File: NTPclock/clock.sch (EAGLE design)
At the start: 27 parts, among them IC1 MAX7219CNG

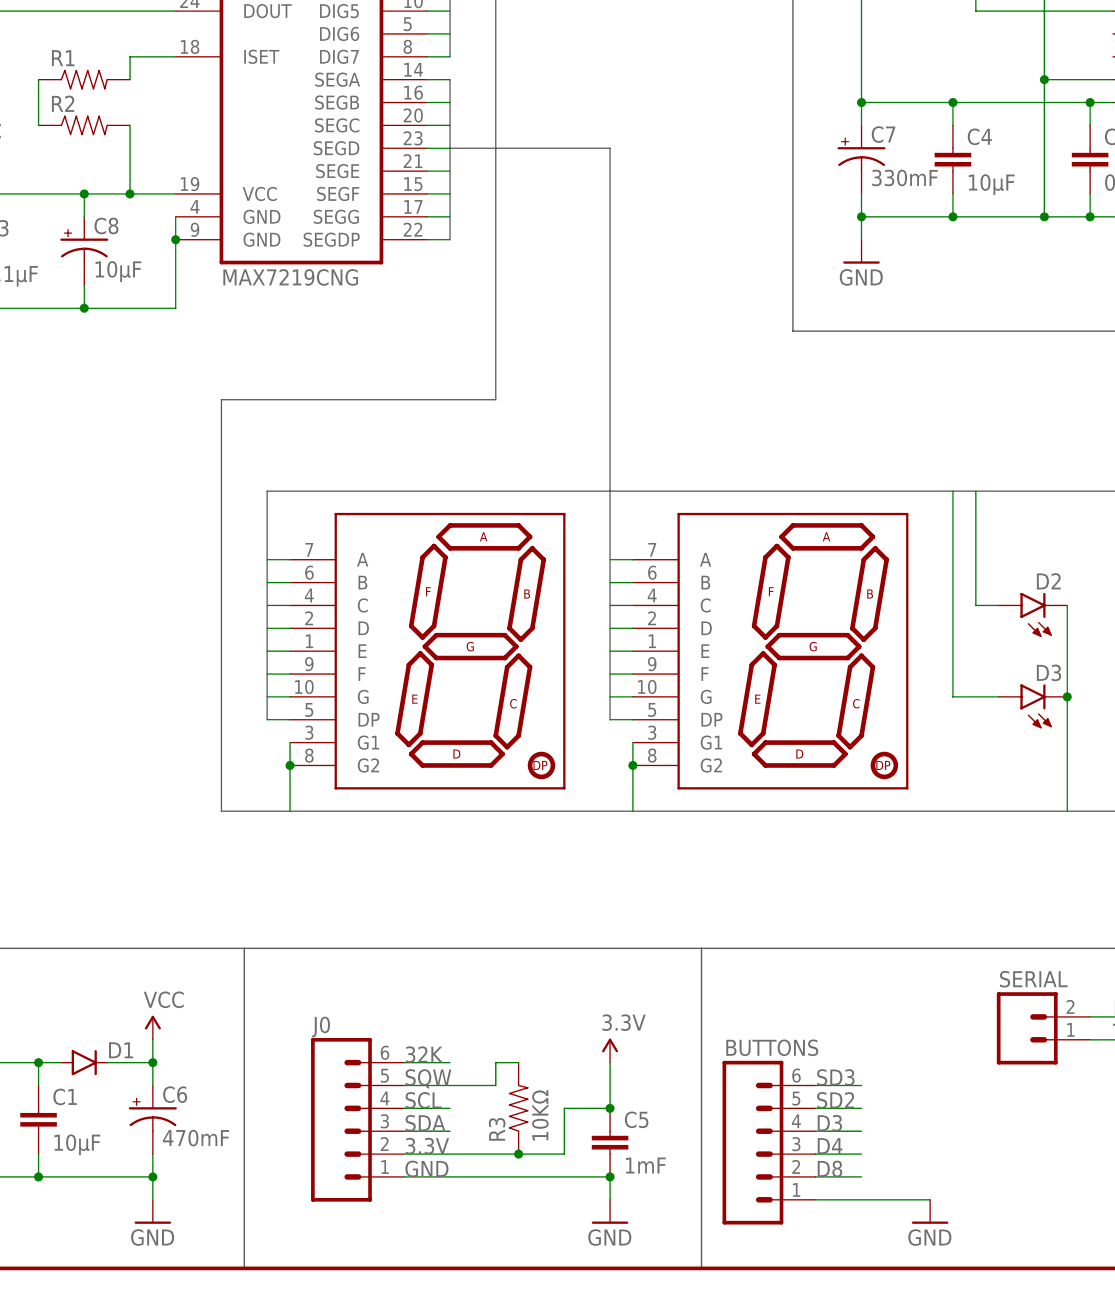
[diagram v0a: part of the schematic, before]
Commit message: Unit fixes
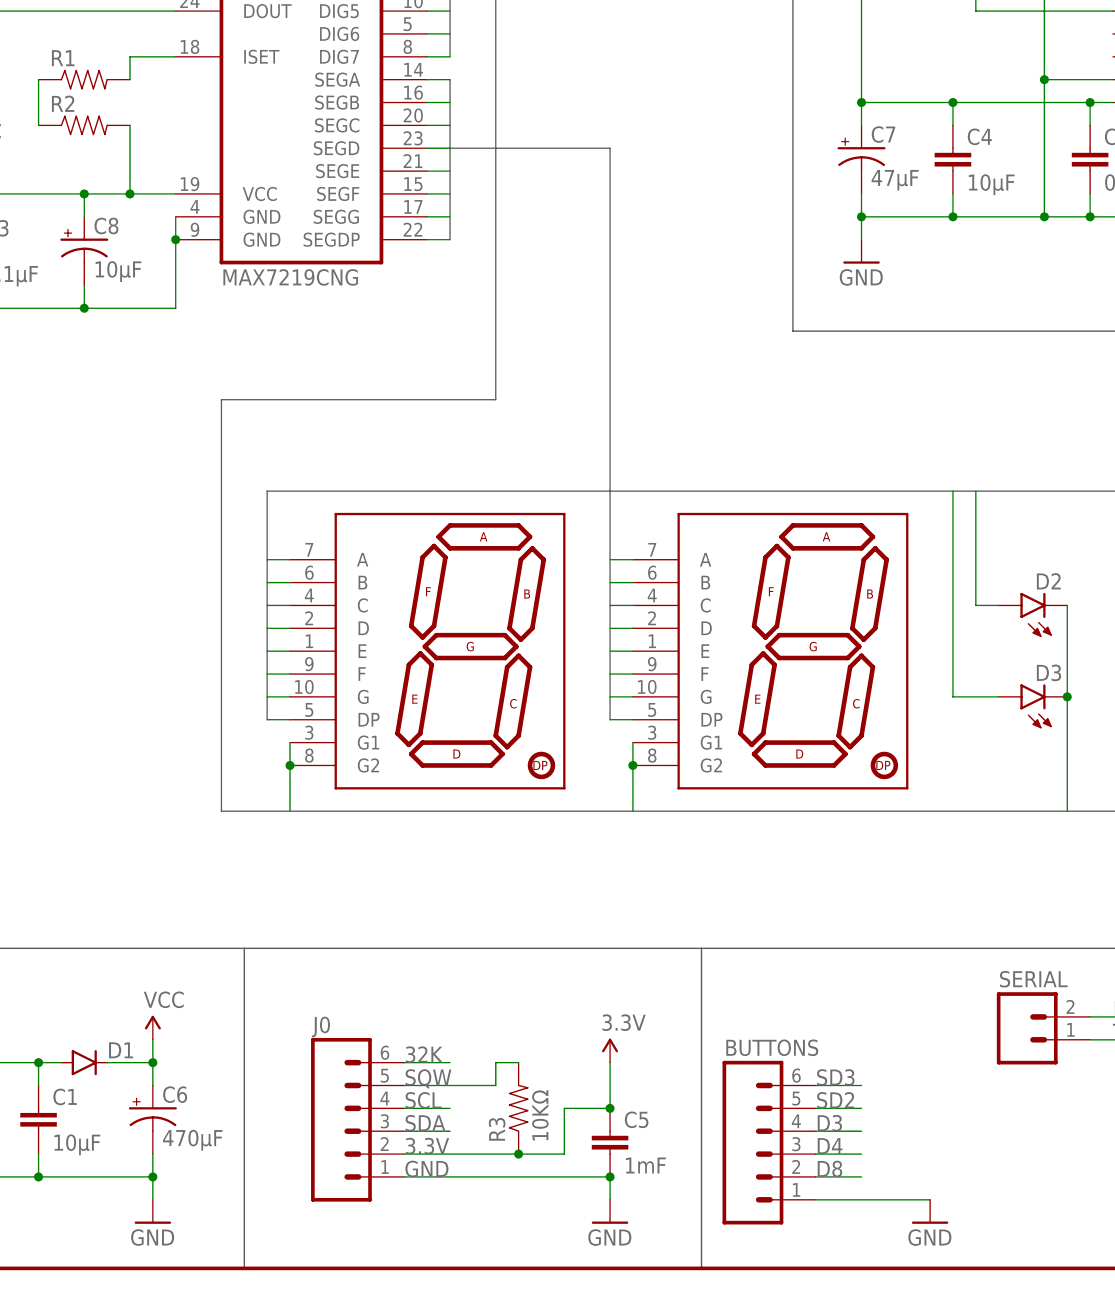
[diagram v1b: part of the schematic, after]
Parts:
- C6: value 470mF -> 470μF
- C7: value 330mF -> 47μF
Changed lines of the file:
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@@
 <part name="C4" library="SparkFun-Capacitors" deviceset="CAP" device="1206" value="10μF"/>
 <part name="C5" library="SparkFun-Capacitors" deviceset="CAP" device="1206" value="1mF"/>
-<part name="C6" library="SparkFun-Capacitors" deviceset="CAP_POL" device="PTH1" value="470mF"/>
-<part name="C7" library="SparkFun-Capacitors" deviceset="CAP_POL" device="PTH1" value="330mF"/>
+<part name="C6" library="SparkFun-Capacitors" deviceset="CAP_POL" device="PTH1" value="470μF"/>
+<part name="C7" library="SparkFun-Capacitors" deviceset="CAP_POL" device="PTH1" value="47μF"/>
 <part name="C8" library="SparkFun-Capacitors" deviceset="CAP_POL" device="PTH1" value="10μF"/>
 <part name="POWER" library="SparkFun-Connectors" deviceset="M02" device="JST-PTH-VERT"/>

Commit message: Add v1.0 logo to board
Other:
- note added: "1.0"
- note removed: "1.1"
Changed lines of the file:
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@@
 <wire x1="215.9" y1="53.34" x2="129.54" y2="53.34" width="0.1524" layer="97"/>
 <wire x1="129.54" y1="53.34" x2="129.54" y2="134.62" width="0.1524" layer="97"/>
-<text x="264.16" y="-43.18" size="1.778" layer="97">1.1</text>
+<text x="264.16" y="-43.18" size="1.778" layer="97">1.0</text>
 <text x="193.04" y="-43.18" size="1.778" layer="97">Joshua Villwock</text>
 <wire x1="215.9" y1="134.62" x2="215.9" y2="53.34" width="0.1524" layer="97"/>

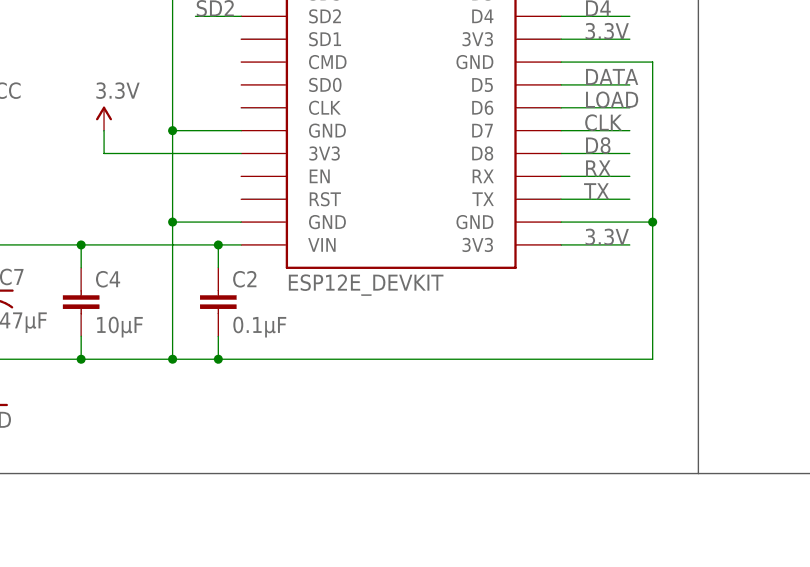
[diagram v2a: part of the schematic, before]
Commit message: Begin updating the Board file for the cheaper V3
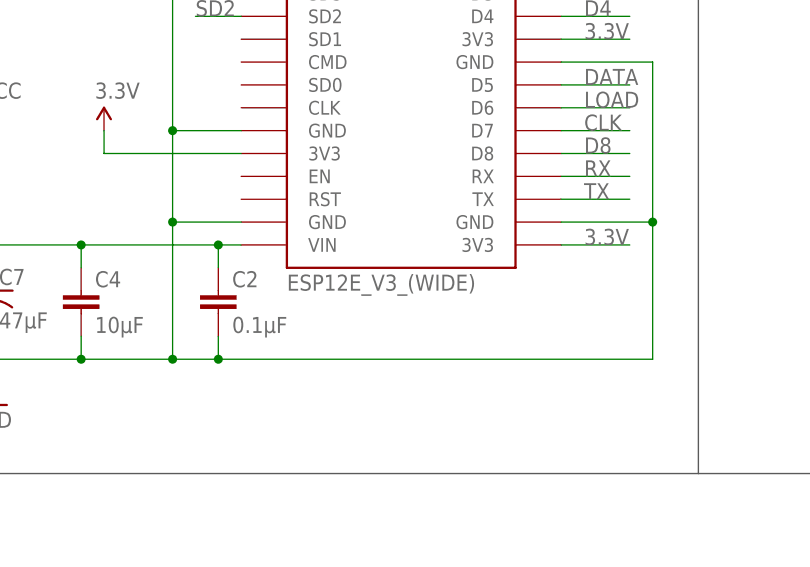
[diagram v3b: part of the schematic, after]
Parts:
- NODEMCU.V3: value ESP12E_DEVKIT -> ESP12E_V3_(WIDE); device NODEMCUv1:ESP12E_DEVKIT -> NODEMCUv1:ESP12E_V3_(WIDE)
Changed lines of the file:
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@@
 </classes>
 <parts>
-<part name="NODEMCU.V3" library="NODEMCUv1" deviceset="ESP12E_DEVKIT" device="" value="ESP12E_DEVKIT"/>
+<part name="NODEMCU.V3" library="NODEMCUv1" deviceset="ESP12E_V3_(WIDE)" device="" value="ESP12E_V3_(WIDE)"/>
 <part name="IC1" library="max7219" deviceset="MAX7219CNG" device=""/>
 <part name="R1" library="SparkFun-Resistors" deviceset="RESISTOR" device="1206"/>

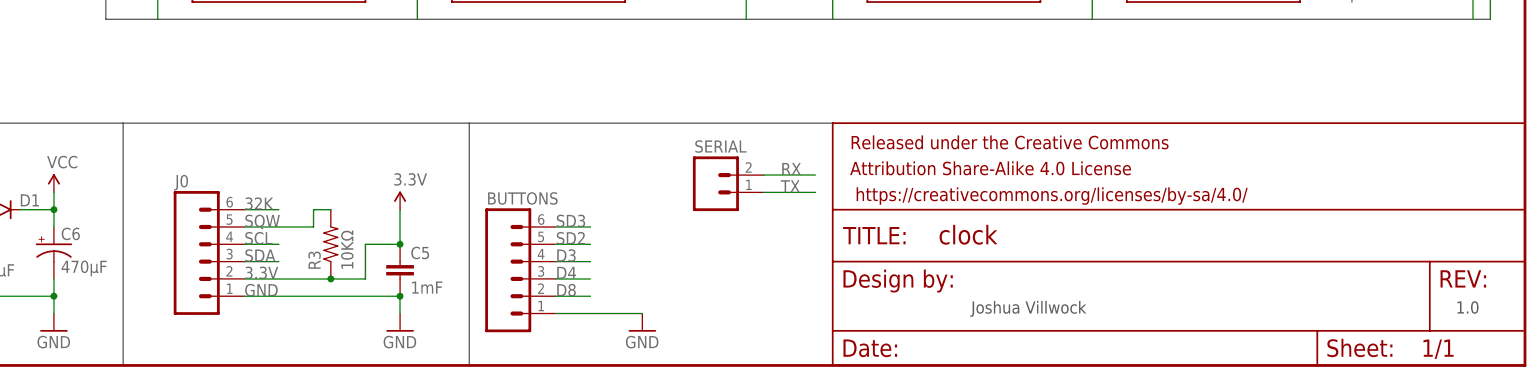
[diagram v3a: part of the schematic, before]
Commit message: Updated NTPclock for new fotprint
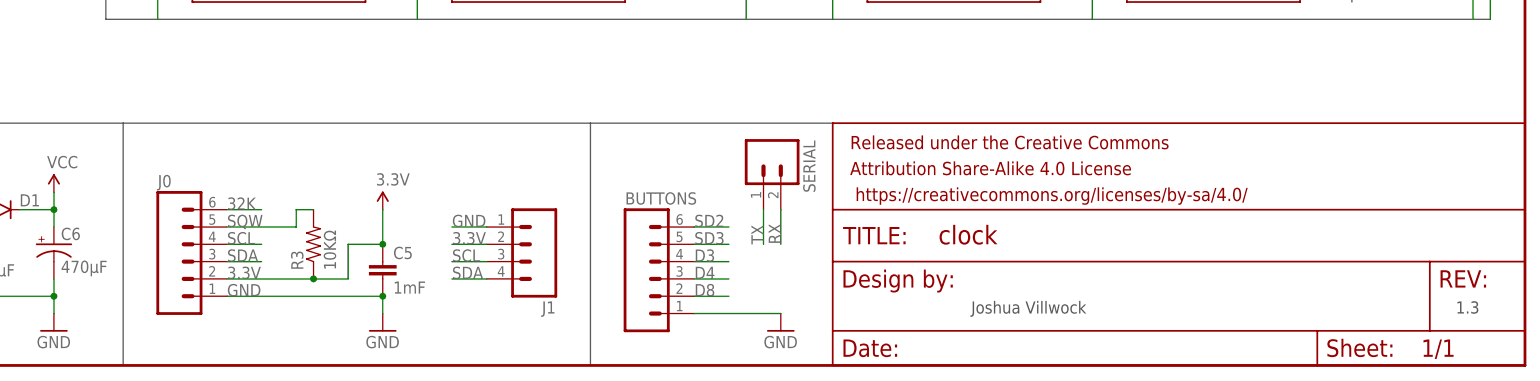
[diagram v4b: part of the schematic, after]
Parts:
- added J1: (no value), SparkFun-Connectors:M04POLAR
- POWER: device SparkFun-Connectors:M02JST-PTH-VERT -> SparkFun-Connectors:M02POLAR_LOCK
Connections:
- net 3.3V: now also J1.2
- net GND: now also J1.1
- net SCL: now also J1.3
- net SD2: now also BUTTONS.6; no longer BUTTONS.5
- net SD3: now also BUTTONS.5; no longer BUTTONS.6
- net SDA: now also J1.4
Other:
- note added: "1.3"
- note removed: "1.0"
- moved on the sheet: BUTTONS, C5, J0, R3, SERIAL
